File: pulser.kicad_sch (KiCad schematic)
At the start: 91 parts, among them J10 CONSMA002-SMD, J16 Conn_02x04_Odd_Even, J18 Conn_01x02_Pin, J19 Conn_01x02_Pin, J20 Conn_01x02_Pin, J21 Conn_01x02_Pin, J22 Conn_01x02_Pin, J23 Conn_01x02_Pin, J24 Conn_01x02_Pin, J25 Conn_01x02_Pin, J28 Conn_02x04_Odd_Even, J3 CONSMA002-SMD, J4 CONSMA002-SMD, J5 CONSMA002-SMD, J6 CONSMA002-SMD, J7 CONSMA002-SMD, J8 CONSMA002-SMD, J9 CONSMA002-SMD, U10 TLV9354IDR, U11 TLV9354IDR, U2 DSC1001DI2-125.0000T, U3 MAX14808ETK_

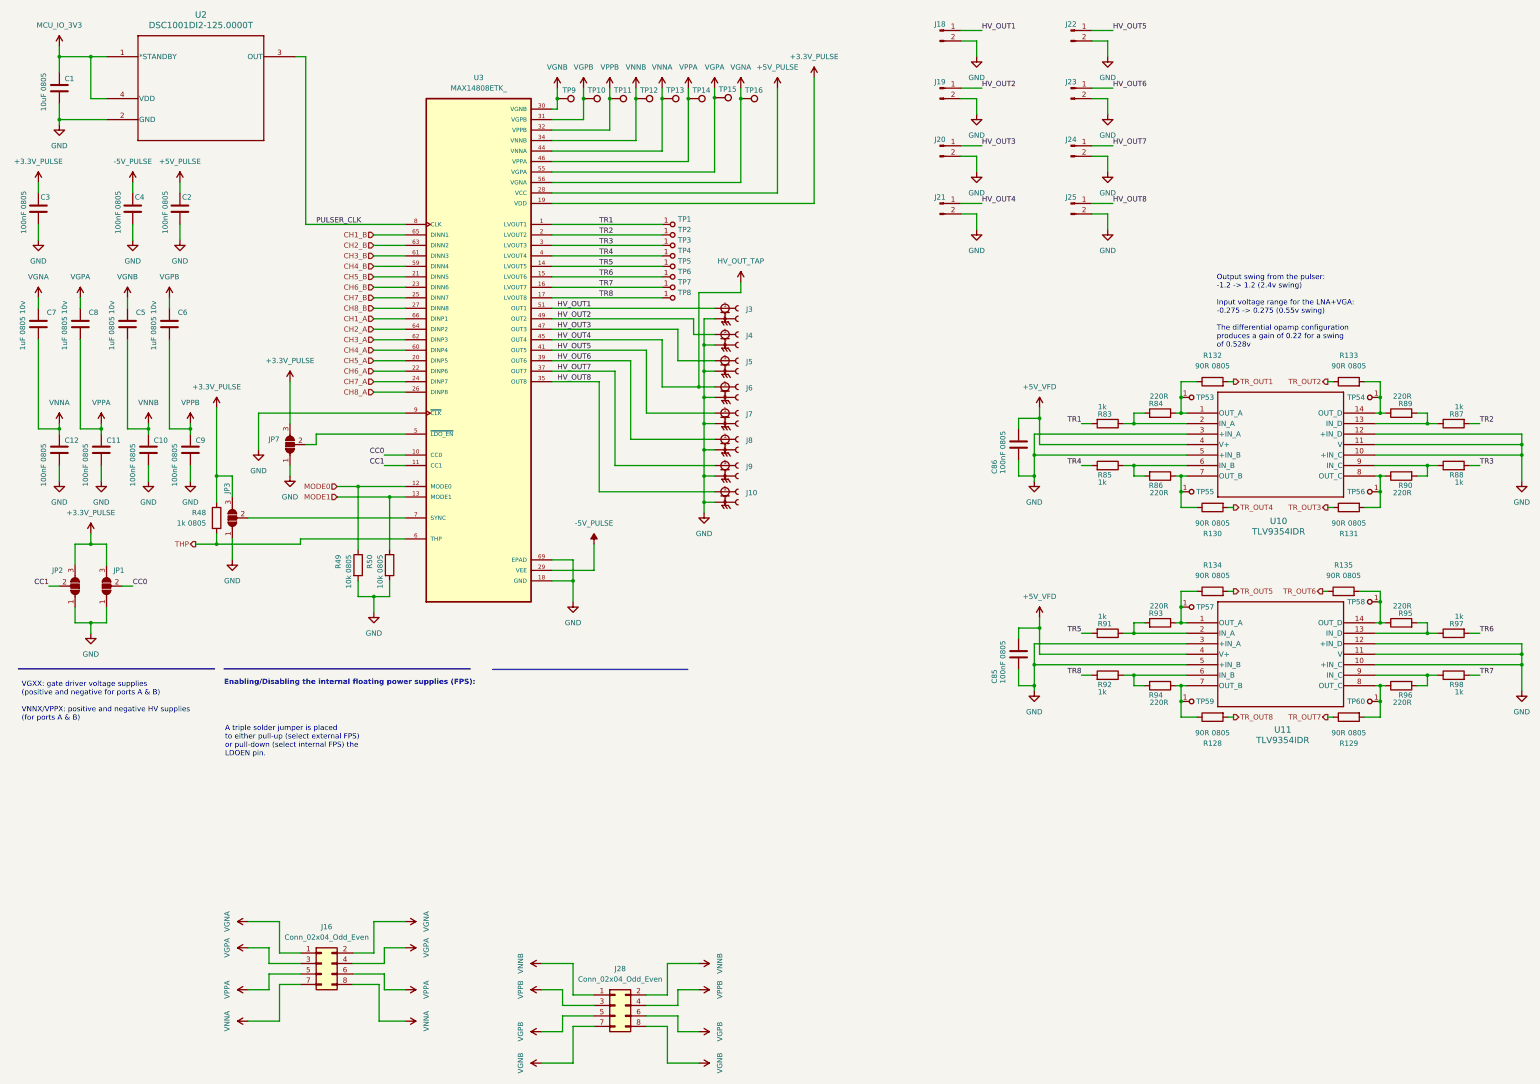
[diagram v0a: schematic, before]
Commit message: added test points & fuse
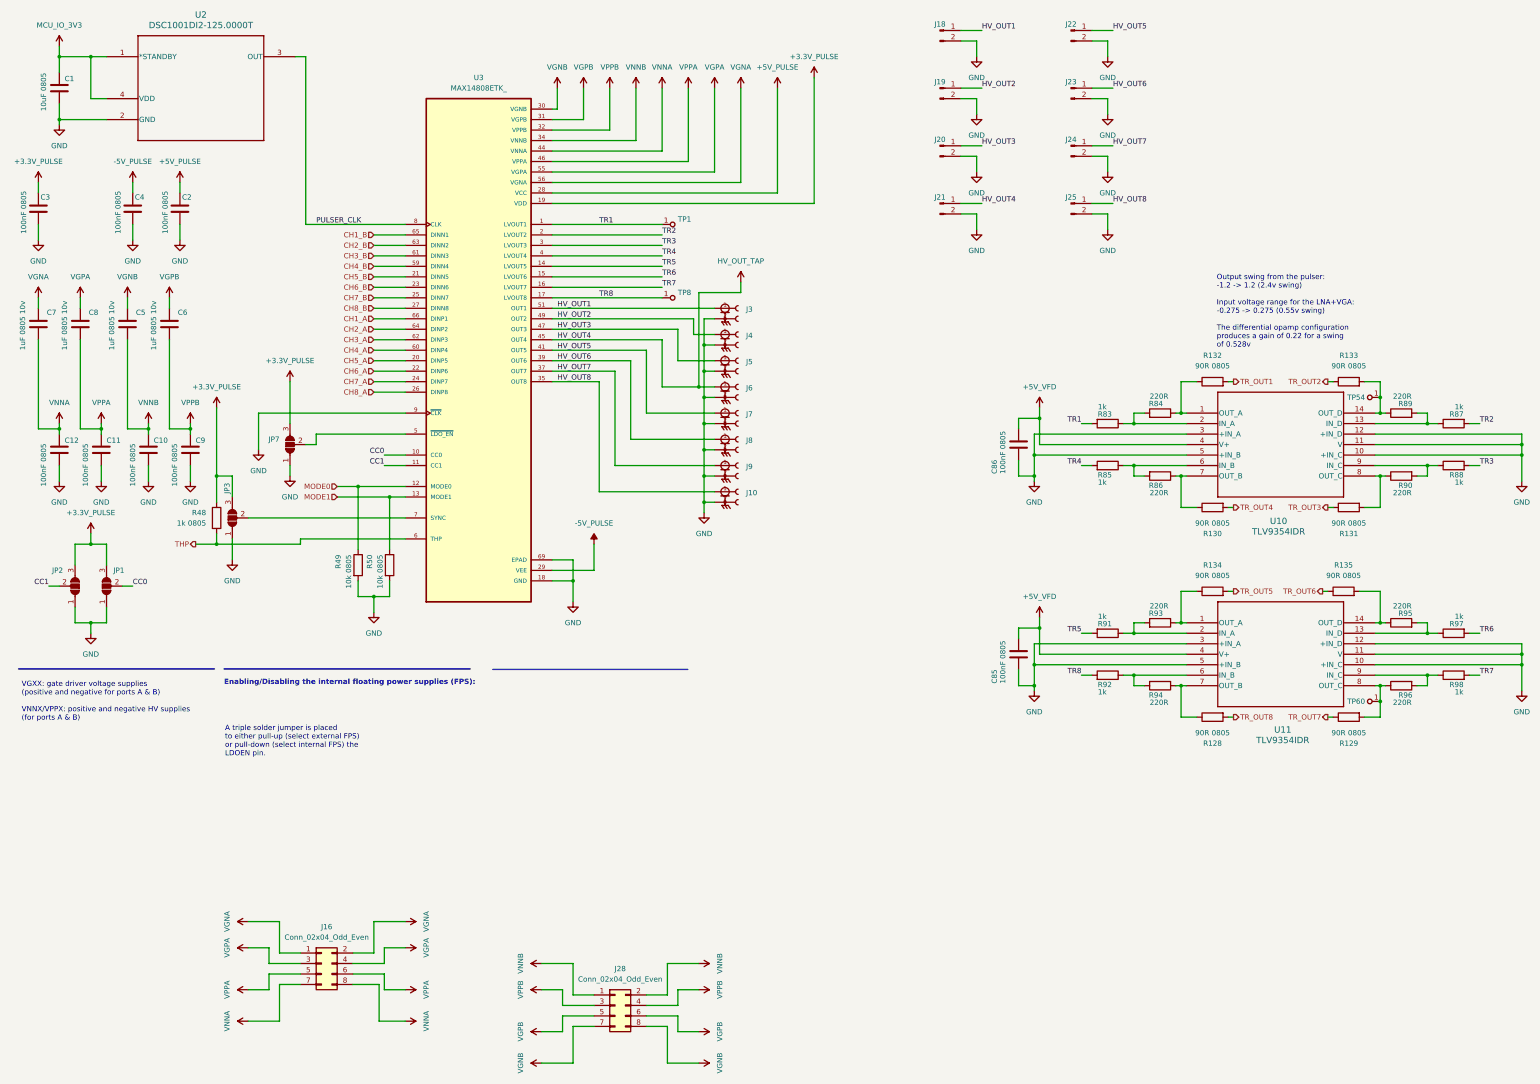
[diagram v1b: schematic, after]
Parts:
- removed TP10, TP11, TP12, TP13, TP14, TP15, TP16, TP9: TestPoint, TestPoint:TestPoint_Pad_D1.5mm, symbol Connector:TestPoint
- removed TP2, TP3, TP4, TP5, TP53, TP55, TP56, TP57, TP58, TP59, TP6, TP7: RCT-0C, digikey-footprints:PROBE_PAD_0805, symbol dk_Test-Points:RCT-0C

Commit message: DONE! Added ESD protection & finalized everything before, this thing is ready for production
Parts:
- added D11, D12: ESD8104MUTAG, ESD8104MUTAG:DIO_ESD8104MUTAG, symbol ESD8104MUTAG:ESD8104MUTAG
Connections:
- net GND: now also D11.3 (GND), D11.8 (GND), D12.3 (GND), D12.8 (GND)
- net VGNA: now also D12.1
- net VGNB: now also D11.5
- net VGPA: now also D12.2
- net VGPB: now also D11.4
- net VNNA: now also D12.5
- net VNNB: now also D11.1
- net VPPA: now also D12.4
- net VPPB: now also D11.2

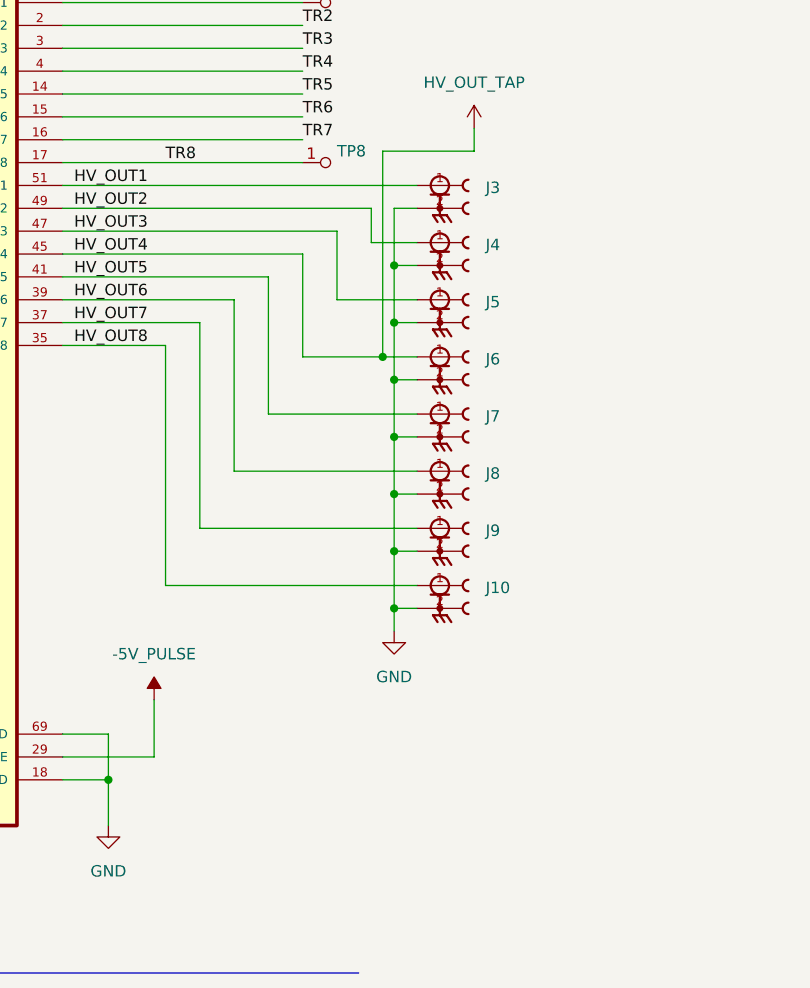
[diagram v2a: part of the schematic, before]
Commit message: Several finishing updates to fit stocks & changed SMA from SMD to THT, updated schematics too
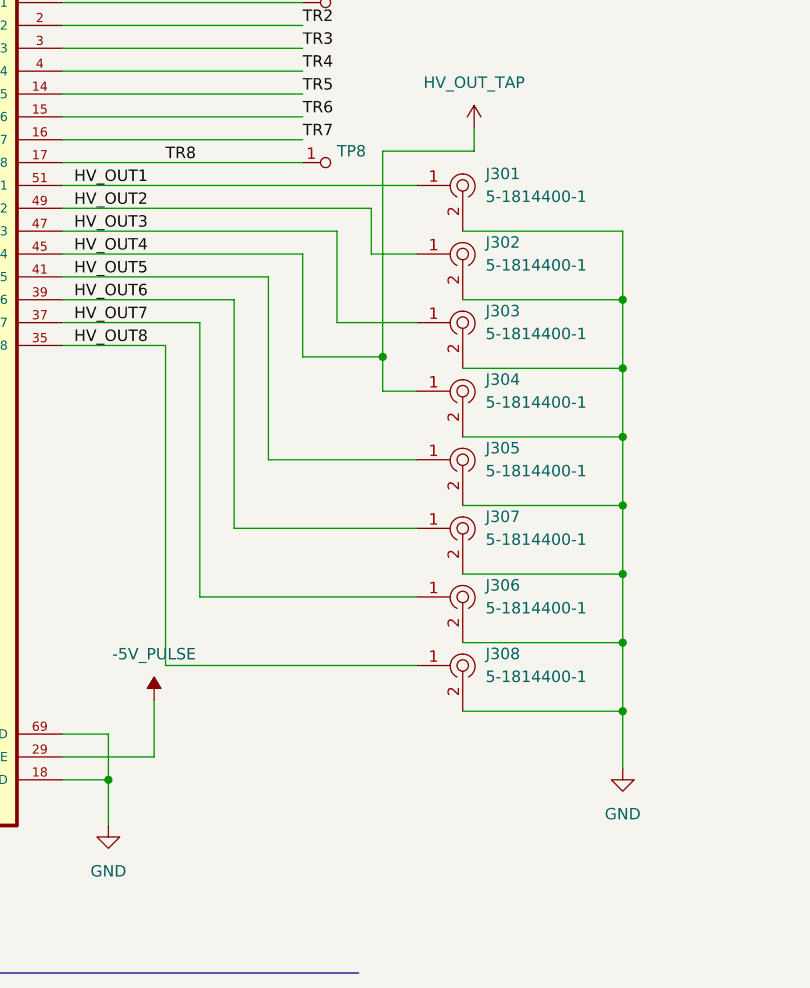
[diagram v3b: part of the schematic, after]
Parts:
- removed J10, J3, J4, J5, J6, J7, J8, J9: CONSMA002-SMD, CONSMA002-SMD:TE_CONSMA002-SMD, symbol CONSMA002-SMD:CONSMA002-SMD
- added J301, J302, J303, J304, J305, J306, J307, J308: 5-1814400-1, digikey-footprints:RF_SMA_RightAngle_5-1814400-1, symbol dk_Coaxial-Connectors-RF:5-1814400-1
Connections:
- net GND: now also J301.2, J302.2, J303.2, J304.2, J305.2, J306.2, J307.2, J308.2
- net HV_OUT1: now also J301.1
- net HV_OUT2: now also J302.1
- net HV_OUT3: now also J303.1
- net HV_OUT5: now also J305.1
- net HV_OUT6: now also J307.1
- net HV_OUT7: now also J306.1
- net HV_OUT8: now also J308.1
- net HV_OUT_TAP: now also J304.1
